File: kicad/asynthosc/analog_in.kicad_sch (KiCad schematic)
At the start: 9 parts, among them J4 AudioJack3, U3 MCP6004, U4 MCP6004

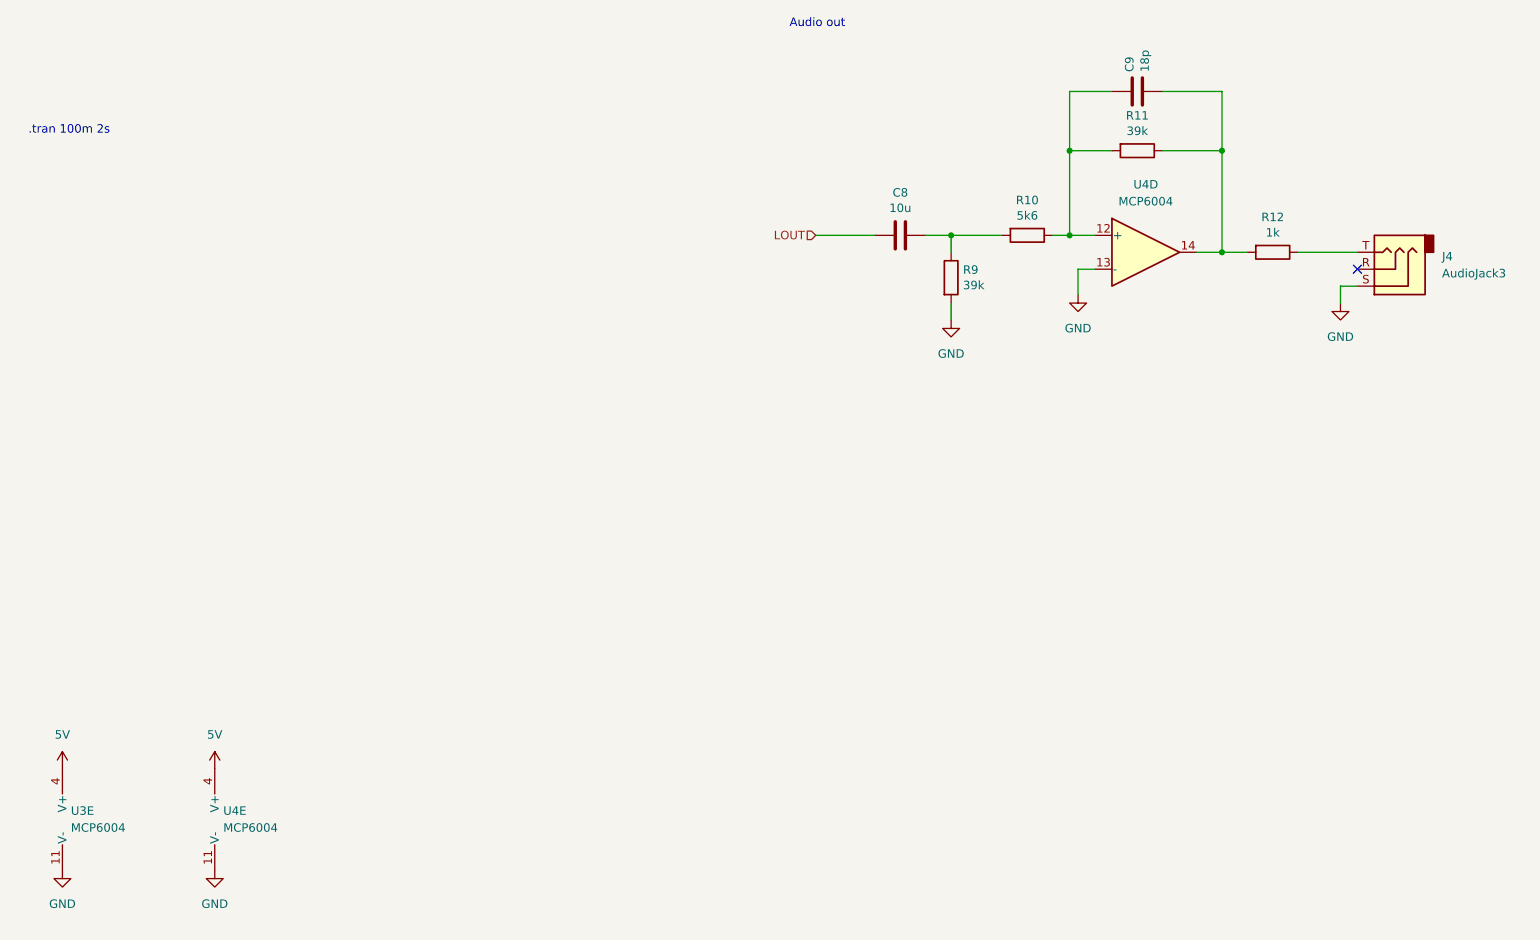
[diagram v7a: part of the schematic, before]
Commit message: bom: update bom for lcsc
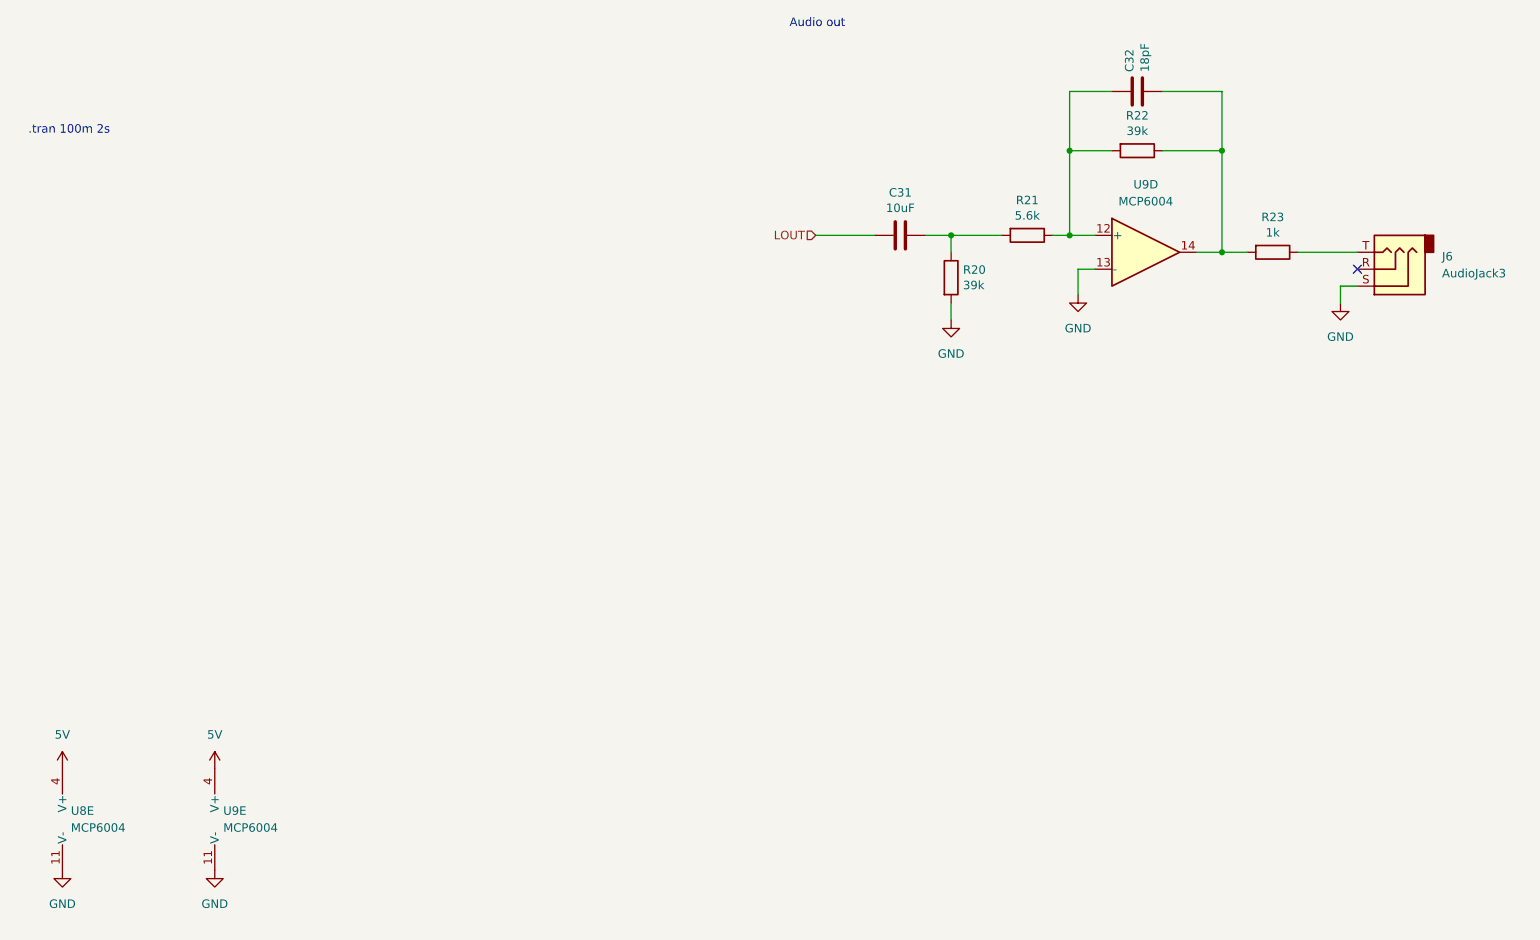
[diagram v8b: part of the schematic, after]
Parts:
- C31: renamed from C8; value 10u -> 10uF
- C32: renamed from C9; value 18p -> 18pF
- R20: renamed from R9; RefNum (none) -> _generic_
- R21: renamed from R10; value 5k6 -> 5.6k; RefNum (none) -> _generic_
- R22: renamed from R11; RefNum (none) -> _generic_
- R23: renamed from R12; RefNum (none) -> _generic_
- U8: renamed from U3; RefNum MCP6004 -> MCP6004T-E/ST
- U9: renamed from U4; RefNum MCP6004 -> MCP6004T-E/ST
- renumbered J4 to J6
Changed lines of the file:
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@@
 		(on_board yes)
 		(dnp no)
-		(property "Reference" "C8"
+		(property "Reference" "C31"
 			(at 154.94 55.8292 90)
 			(effects
@@
 			)
 		)
-		(property "Value" "10u"
+		(property "Value" "10uF"
 			(at 154.94 58.1406 90)
 			(effects
@@
 			(project "asynthosc"
 				(path "/d73e377a-a016-415f-8824-91cc6e4907b9/5f8430bb-1923-4d76-b418-f207310879ec"
-					(reference "C8")
+					(reference "C31")
 					(unit 1)
 				)
@@
 		(dnp no)
 		(fields_autoplaced yes)
-		(property "Reference" "#PWR028"
+		(property "Reference" "#PWR062"
 			(at 220.98 78.74 0)
 			(effects
@@
 			(project "asynthosc"
 				(path "/d73e377a-a016-415f-8824-91cc6e4907b9/5f8430bb-1923-4d76-b418-f207310879ec"
-					(reference "#PWR028")
+					(reference "#PWR062")
 					(unit 1)
 				)
@@
 		(dnp no)
 		(fields_autoplaced yes)
-		(property "Reference" "#PWR018"
+		(property "Reference" "#PWR058"
 			(at 52.07 146.05 0)
 			(effects
@@
 			(project "asynthosc"
 				(path "/d73e377a-a016-415f-8824-91cc6e4907b9/5f8430bb-1923-4d76-b418-f207310879ec"
-					(reference "#PWR018")
+					(reference "#PWR058")
 					(unit 1)
 				)
@@
 		(dnp no)
 		(fields_autoplaced yes)
-		(property "Reference" "#PWR026"
+		(property "Reference" "#PWR060"
 			(at 162.56 81.28 0)
 			(effects
@@
 			(project "asynthosc"
 				(path "/d73e377a-a016-415f-8824-91cc6e4907b9/5f8430bb-1923-4d76-b418-f207310879ec"
-					(reference "#PWR026")
+					(reference "#PWR060")
 					(unit 1)
 				)
@@
 		(dnp no)
 		(fields_autoplaced yes)
-		(property "Reference" "#PWR012"
+		(property "Reference" "#PWR056"
 			(at 29.21 146.05 0)
 			(effects
@@
 			(project "asynthosc"
 				(path "/d73e377a-a016-415f-8824-91cc6e4907b9/5f8430bb-1923-4d76-b418-f207310879ec"
-					(reference "#PWR012")
+					(reference "#PWR056")
 					(unit 1)
 				)
@@
 		(dnp no)
 		(fields_autoplaced yes)
-		(property "Reference" "#PWR027"
+		(property "Reference" "#PWR061"
 			(at 181.61 77.47 0)
 			(effects
@@
 			(project "asynthosc"
 				(path "/d73e377a-a016-415f-8824-91cc6e4907b9/5f8430bb-1923-4d76-b418-f207310879ec"
-					(reference "#PWR027")
+					(reference "#PWR061")
 					(unit 1)
 				)
@@
 		(on_board yes)
 		(dnp no)
-		(property "Reference" "R9"
+		(property "Reference" "R20"
 			(at 164.338 67.4116 0)
 			(effects
@@
 			)
 		)
+		(property "RefNum" "_generic_"
+			(at 162.56 68.58 0)
+			(effects
+				(font
+					(size 1.27 1.27)
+				)
+				(hide yes)
+			)
+		)
 		(pin "1"
 		)
@@
 			(project "asynthosc"
 				(path "/d73e377a-a016-415f-8824-91cc6e4907b9/5f8430bb-1923-4d76-b418-f207310879ec"
-					(reference "R9")
+					(reference "R20")
 					(unit 1)
 				)
@@
 		(dnp no)
 		(fields_autoplaced yes)
-		(property "Reference" "U3"
+		(property "Reference" "U8"
 			(at 30.48 148.5899 0)
 			(effects
@@
 			)
 		)
-		(property "RefNum" "MCP6004"
+		(property "RefNum" " MCP6004T-E/ST"
 			(at 31.75 149.86 0)
 			(effects
@@
 			(project "asynthosc"
 				(path "/d73e377a-a016-415f-8824-91cc6e4907b9/5f8430bb-1923-4d76-b418-f207310879ec"
-					(reference "U3")
+					(reference "U8")
 					(unit 5)
 				)
@@
 		(on_board yes)
 		(dnp no)
-		(property "Reference" "R10"
+		(property "Reference" "R21"
 			(at 173.99 56.9722 90)
 			(effects
@@
 			)
 		)
-		(property "Value" "5k6"
+		(property "Value" "5.6k"
 			(at 173.99 59.2836 90)
 			(effects
@@
 			)
 		)
+		(property "RefNum" "_generic_"
+			(at 173.99 62.23 0)
+			(effects
+				(font
+					(size 1.27 1.27)
+				)
+				(hide yes)
+			)
+		)
 		(pin "1"
 		)
@@
 			(project "asynthosc"
 				(path "/d73e377a-a016-415f-8824-91cc6e4907b9/5f8430bb-1923-4d76-b418-f207310879ec"
-					(reference "R10")
+					(reference "R21")
 					(unit 1)
 				)
@@
 		(on_board yes)
 		(dnp no)
-		(property "Reference" "R11"
+		(property "Reference" "R22"
 			(at 190.5 44.2722 90)
 			(effects
@@
 			)
 		)
+		(property "RefNum" "_generic_"
+			(at 190.5 49.53 0)
+			(effects
+				(font
+					(size 1.27 1.27)
+				)
+				(hide yes)
+			)
+		)
 		(pin "1"
 		)
@@
 			(project "asynthosc"
 				(path "/d73e377a-a016-415f-8824-91cc6e4907b9/5f8430bb-1923-4d76-b418-f207310879ec"
-					(reference "R11")
+					(reference "R22")
 					(unit 1)
 				)
@@
 		(dnp no)
 		(fields_autoplaced yes)
-		(property "Reference" "J4"
+		(property "Reference" "J6"
 			(at 236.22 65.4049 0)
 			(effects
@@
 			(project "asynthosc"
 				(path "/d73e377a-a016-415f-8824-91cc6e4907b9/5f8430bb-1923-4d76-b418-f207310879ec"
-					(reference "J4")
+					(reference "J6")
 					(unit 1)
 				)
@@
 		(dnp no)
 		(fields_autoplaced yes)
-		(property "Reference" "#PWR013"
+		(property "Reference" "#PWR057"
 			(at 29.21 163.83 0)
 			(effects
@@
 			(project "asynthosc"
 				(path "/d73e377a-a016-415f-8824-91cc6e4907b9/5f8430bb-1923-4d76-b418-f207310879ec"
-					(reference "#PWR013")
+					(reference "#PWR057")
 					(unit 1)
 				)
@@
 		(on_board yes)
 		(dnp no)
-		(property "Reference" "R12"
+		(property "Reference" "R23"
 			(at 210.82 59.5122 90)
 			(effects
@@
 			)
 		)
+		(property "RefNum" "_generic_"
+			(at 210.82 64.77 0)
+			(effects
+				(font
+					(size 1.27 1.27)
+				)
+				(hide yes)
+			)
+		)
 		(pin "1"
 		)
@@
 			(project "asynthosc"
 				(path "/d73e377a-a016-415f-8824-91cc6e4907b9/5f8430bb-1923-4d76-b418-f207310879ec"
-					(reference "R12")
+					(reference "R23")
 					(unit 1)
 				)
@@
 		(dnp no)
 		(fields_autoplaced yes)
-		(property "Reference" "U4"
+		(property "Reference" "U9"
 			(at 53.34 148.5899 0)
 			(effects
@@
 			)
 		)
-		(property "RefNum" "MCP6004"
+		(property "RefNum" " MCP6004T-E/ST"
 			(at 54.61 149.86 0)
 			(effects
@@
 			(project ""
 				(path "/d73e377a-a016-415f-8824-91cc6e4907b9/5f8430bb-1923-4d76-b418-f207310879ec"
-					(reference "U4")
+					(reference "U9")
 					(unit 5)
 				)
@@
 		(on_board yes)
 		(dnp no)
-		(property "Reference" "C9"
+		(property "Reference" "C32"
 			(at 189.3316 37.719 0)
 			(effects
@@
 			)
 		)
-		(property "Value" "18p"
+		(property "Value" "18pF"
 			(at 191.643 37.719 0)
 			(effects
@@
 			(project "asynthosc"
 				(path "/d73e377a-a016-415f-8824-91cc6e4907b9/5f8430bb-1923-4d76-b418-f207310879ec"
-					(reference "C9")
+					(reference "C32")
 					(unit 1)
 				)
@@
 		(dnp no)
 		(fields_autoplaced yes)
-		(property "Reference" "#PWR019"
+		(property "Reference" "#PWR059"
 			(at 52.07 163.83 0)
 			(effects
@@
 			(project ""
 				(path "/d73e377a-a016-415f-8824-91cc6e4907b9/5f8430bb-1923-4d76-b418-f207310879ec"
-					(reference "#PWR019")
+					(reference "#PWR059")
 					(unit 1)
 				)
@@
 		(dnp no)
 		(fields_autoplaced yes)
-		(property "Reference" "U4"
+		(property "Reference" "U9"
 			(at 191.77 54.61 0)
 			(effects
@@
 			)
 		)
-		(property "RefNum" "MCP6004"
+		(property "RefNum" " MCP6004T-E/ST"
 			(at 191.77 64.77 0)
 			(effects
@@
 			(project "asynthosc"
 				(path "/d73e377a-a016-415f-8824-91cc6e4907b9/5f8430bb-1923-4d76-b418-f207310879ec"
-					(reference "U4")
+					(reference "U9")
 					(unit 4)
 				)
